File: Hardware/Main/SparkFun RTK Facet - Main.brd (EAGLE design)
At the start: 60 x 43 mm, 124 parts, among them J1 QWIIC_RIGHT_ANGLE, J2 U.FL, J9 CORTEX_JTAG_DEBUG_PTH, Q2 MBT3904DW1T1, Q3 SIL2308, U1 74HC4052D, U10 MCP73833, U12 AP2112K-3.3, U2 3.3V, U3 U-BLOX_ZED-F9P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

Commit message: Change to NO jumper for I2C pullups
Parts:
- added U$15, U$16: (no value), output:RTK5#SVG0
- C20: value 22uF -> 10uF
- JP7: value JUMPER-SMT_3_2-NC_TRACE_SILK -> JUMPER-SMT_3_NO_SILK; device SparkFun-Jumpers:SMT-JUMPER_3_2-NC_TRACE_SILK -> SparkFun-Jumpers:SMT-JUMPER_3_NO_SILK
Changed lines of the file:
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@@
 <layers>
 <layer number="1" name="Top/Horz" color="4" fill="1" visible="yes" active="yes"/>
-<layer number="2" name="GND/Horz" color="1" fill="3" visible="yes" active="yes"/>
-<layer number="15" name="3.3V/Vert" color="4" fill="6" visible="yes" active="yes"/>
+<layer number="2" name="GND/Horz" color="1" fill="3" visible="no" active="yes"/>
+<layer number="15" name="3.3V/Vert" color="4" fill="6" visible="no" active="yes"/>
 <layer number="16" name="Bottom/Vert" color="1" fill="1" visible="yes" active="yes"/>
 <layer number="17" name="Pads" color="2" fill="1" visible="yes" active="yes"/>
@@
 <layer number="23" name="tOrigins" color="15" fill="1" visible="yes" active="yes"/>
 <layer number="24" name="bOrigins" color="15" fill="1" visible="yes" active="yes"/>
-<layer number="25" name="tNames" color="7" fill="1" visible="yes" active="yes"/>
-<layer number="26" name="bNames" color="7" fill="1" visible="yes" active="yes"/>
-<layer number="27" name="tValues" color="7" fill="1" visible="yes" active="yes"/>
-<layer number="28" name="bValues" color="7" fill="1" visible="yes" active="yes"/>
-<layer number="29" name="tStop" color="7" fill="3" visible="yes" active="yes"/>
-<layer number="30" name="bStop" color="7" fill="6" visible="yes" active="yes"/>
-<layer number="31" name="tCream" color="7" fill="4" visible="yes" active="yes"/>
-<layer number="32" name="bCream" color="7" fill="5" visible="yes" active="yes"/>
-<layer number="33" name="tFinish" color="6" fill="3" visible="yes" active="yes"/>
-<layer number="34" name="bFinish" color="6" fill="6" visible="yes" active="yes"/>
-<layer number="35" name="tGlue" color="7" fill="4" visible="yes" active="yes"/>
-<layer number="36" name="bGlue" color="7" fill="5" visible="yes" active="yes"/>
-<layer number="37" name="tTest" color="7" fill="1" visible="yes" active="yes"/>
-<layer number="38" name="bTest" color="7" fill="1" visible="yes" active="yes"/>
-<layer number="39" name="tKeepout" color="4" fill="11" visible="yes" active="yes"/>
-<layer number="40" name="bKeepout" color="1" fill="11" visible="yes" active="yes"/>
-<layer number="41" name="tRestrict" color="4" fill="10" visible="yes" active="yes"/>
-<layer number="42" name="bRestrict" color="1" fill="10" visible="yes" active="yes"/>
-<layer number="43" name="vRestrict" color="2" fill="10" visible="yes" active="yes"/>
-<layer number="44" name="Drills" color="7" fill="1" visible="yes" active="yes"/>
+<layer number="25" name="tNames" color="7" fill="1" visible="no" active="yes"/>
+<layer number="26" name="bNames" color="7" fill="1" visible="no" active="yes"/>
+<layer number="27" name="tValues" color="7" fill="1" visible="no" active="yes"/>
+<layer number="28" name="bValues" color="7" fill="1" visible="no" active="yes"/>
+<layer number="29" name="tStop" color="7" fill="3" visible="no" active="yes"/>
+<layer number="30" name="bStop" color="7" fill="6" visible="no" active="yes"/>
+<layer number="31" name="tCream" color="7" fill="4" visible="no" active="yes"/>
+<layer number="32" name="bCream" color="7" fill="5" visible="no" active="yes"/>
+<layer number="33" name="tFinish" color="6" fill="3" visible="no" active="yes"/>
+<layer number="34" name="bFinish" color="6" fill="6" visible="no" active="yes"/>
+<layer number="35" name="tGlue" color="7" fill="4" visible="no" active="yes"/>
+<layer number="36" name="bGlue" color="7" fill="5" visible="no" active="yes"/>
+<layer number="37" name="tTest" color="7" fill="1" visible="no" active="yes"/>
+<layer number="38" name="bTest" color="7" fill="1" visible="no" active="yes"/>
+<layer number="39" name="tKeepout" color="4" fill="11" visible="no" active="yes"/>
+<layer number="40" name="bKeepout" color="1" fill="11" visible="no" active="yes"/>
+<layer number="41" name="tRestrict" color="4" fill="10" visible="no" active="yes"/>
+<layer number="42" name="bRestrict" color="1" fill="10" visible="no" active="yes"/>
+<layer number="43" name="vRestrict" color="2" fill="10" visible="no" active="yes"/>
+<layer number="44" name="Drills" color="7" fill="1" visible="no" active="yes"/>
 <layer number="45" name="Holes" color="7" fill="1" visible="yes" active="yes"/>
-<layer number="46" name="Milling" color="3" fill="1" visible="yes" active="yes"/>
-<layer number="47" name="Measures" color="7" fill="1" visible="yes" active="yes"/>
-<layer number="48" name="Document" color="7" fill="1" visible="yes" active="yes"/>
-<layer number="49" name="Reference" color="7" fill="1" visible="yes" active="yes"/>
-<layer number="50" name="dxf" color="7" fill="1" visible="yes" active="yes"/>
+<layer number="46" name="Milling" color="3" fill="1" visible="no" active="yes"/>
+<layer number="47" name="Measures" color="7" fill="1" visible="no" active="yes"/>
+<layer number="48" name="Document" color="7" fill="1" visible="no" active="yes"/>
+<layer number="49" name="Reference" color="7" fill="1" visible="no" active="yes"/>
+<layer number="50" name="dxf" color="7" fill="1" visible="no" active="yes"/>
 <layer number="51" name="tDocu" color="6" fill="1" visible="yes" active="yes"/>
-<layer number="52" name="bDocu" color="7" fill="1" visible="yes" active="yes"/>
+<layer number="52" name="bDocu" color="7" fill="1" visible="no" active="yes"/>
 <layer number="91" name="Nets" color="2" fill="1" visible="no" active="no"/>
 <layer number="92" name="Busses" color="1" fill="1" visible="no" active="no"/>
@@
 <attribute name="VALUE" x="19" y="11.762" size="0.6096" layer="28" font="vector" ratio="20" rot="MR180" align="top-center"/>
 </element>
-<element name="JP7" library="SparkFun-Jumpers" package="SMT-JUMPER_3_2-NC_TRACE_SILK" package3d_urn="urn:adsk.eagle:package:39289/1" value="JUMPER-SMT_3_2-NC_TRACE_SILK" x="22" y="10" smashed="yes" rot="MR270">
+<element name="JP7" library="SparkFun-Jumpers" package="SMT-JUMPER_3_NO_SILK" package3d_urn="urn:adsk.eagle:package:39285/1" value="JUMPER-SMT_3_NO_SILK" x="22" y="10" smashed="yes" rot="MR270">
 <attribute name="NAME" x="20.857" y="10" size="0.6096" layer="26" font="vector" ratio="20" rot="MR270" align="bottom-center"/>
 <attribute name="VALUE" x="23.143" y="10" size="0.6096" layer="28" font="vector" ratio="20" rot="MR270" align="top-center"/>
@@
 <attribute name="VALUE" x="6" y="30.778" size="0.6096" layer="28" font="vector" ratio="20" rot="MR180" align="top-center"/>
 </element>
-<element name="C20" library="SparkFun-Capacitors" package="0603" value="22uF" x="6" y="26" smashed="yes" rot="MR0">
+<element name="C20" library="SparkFun-Capacitors" package="0603" value="10uF" x="6" y="26" smashed="yes" rot="MR0">
 <attribute name="NAME" x="6" y="26.762" size="0.6096" layer="26" font="vector" ratio="20" rot="MR0" align="bottom-center"/>
-<attribute name="PROD_ID" value="CAP-14464" x="11" y="32" size="1.778" layer="28" font="vector" ratio="15" rot="MR0" display="off"/>
-<attribute name="VALUE" x="6" y="25.238" size="0.6096" layer="28" font="vector" ratio="20" rot="MR0" align="top-center"/>
+<attribute name="PROD_ID" value="CAP-11015" x="11" y="32" size="1.778" layer="28" font="vector" ratio="15" rot="MR0" display="off"/>
+<attribute name="VALUE" value="10uF" x="6" y="25.238" size="0.6096" layer="28" font="vector" ratio="20" rot="MR0" align="top-center"/>
 </element>
 <element name="R22" library="SparkFun-Resistors" package="0603" value="10k" x="6" y="24" smashed="yes" rot="MR180">
@@
 <element name="U$13" library="output" package="RTK_FACET0" value="" x="41.45" y="26.175" smashed="yes" rot="MR0"/>
 <element name="U$14" library="output" package="#GND#1" value="" x="52" y="11" smashed="yes" rot="MR270"/>
+<element name="U$15" library="output" package="RTK5#SVG0" value="" x="56.007" y="5.842" smashed="yes"/>
+<element name="U$16" library="output" package="RTK5#SVG0" value="" x="46.99" y="33.274" smashed="yes" rot="MR0"/>
 </elements>
 <signals>
@@
 <contactref element="R7" pad="2"/>
 <contactref element="JP7" pad="3"/>
-<wire x1="22" y1="8.9586" x2="19.8914" y2="8.9586" width="0.127" layer="16"/>
 <wire x1="19.8914" y1="8.9586" x2="19.85" y2="9" width="0.127" layer="16"/>
+<wire x1="22" y1="9.1872" x2="20.12" y2="9.1872" width="0.127" layer="16"/>
+<wire x1="20.12" y1="9.1872" x2="19.8914" y2="8.9586" width="0.127" layer="16"/>
 </signal>
 <signal name="N$4">
 <contactref element="R12" pad="2"/>
 <contactref element="JP7" pad="1"/>
-<wire x1="19.85" y1="11" x2="21.9586" y2="11" width="0.127" layer="16"/>
-<wire x1="21.9586" y1="11" x2="22" y2="11.0414" width="0.127" layer="16"/>
+<wire x1="22" y1="10.8128" x2="20.0372" y2="10.8128" width="0.127" layer="16"/>
+<wire x1="20.0372" y1="10.8128" x2="19.85" y2="11" width="0.127" layer="16"/>
 </signal>
 <signal name="N$5">

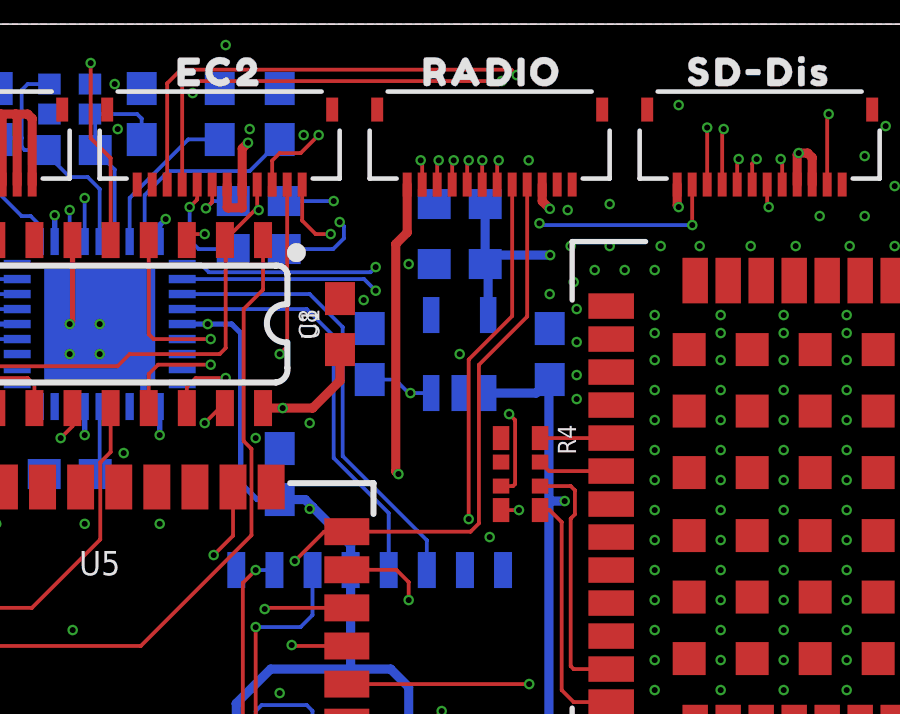
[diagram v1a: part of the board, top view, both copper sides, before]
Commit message: Double up 3.3V rail on Radio connector.
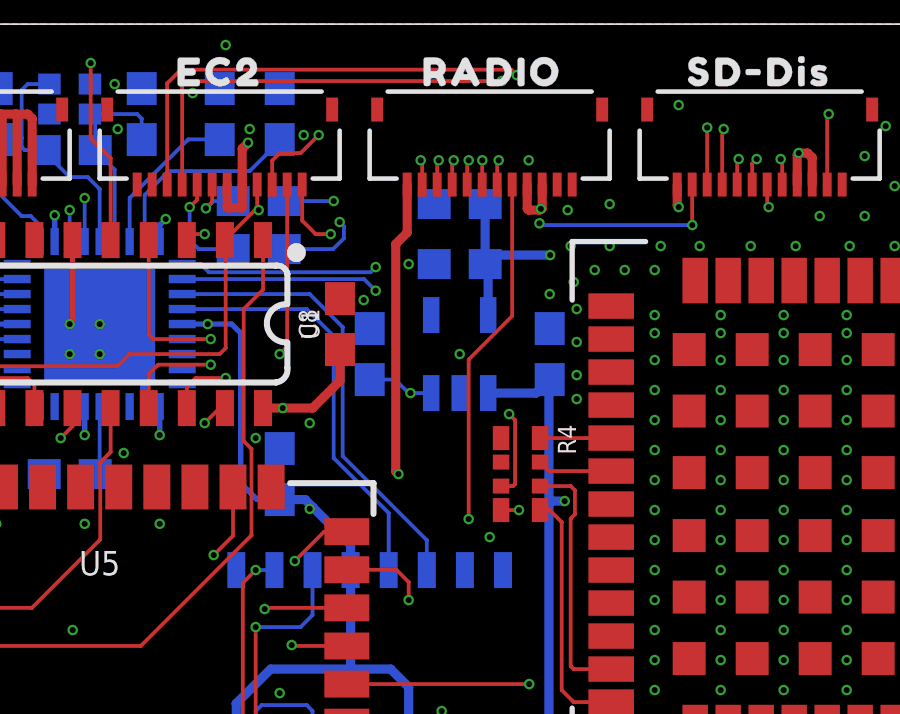
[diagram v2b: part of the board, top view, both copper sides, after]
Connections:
- removed net ESP_12/MTDI/RADIO_NI: J10.4, J9.8, U5.14
- new net ESP_12/MTDI: J9.8, U5.14
- net 3.3V: now also J10.4
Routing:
- net ESP_12/MTDI/RADIO_NI: track 43.0 -> 0.00 mm, vias 2 -> 0
- net ESP_12/MTDI: track 0.00 -> 26.5 mm, vias 0 -> 2
- net 3.3V: track 29.8 -> 31.0 mm
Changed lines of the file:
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@@
 <layers>
 <layer number="1" name="Top/Horz" color="4" fill="1" visible="yes" active="yes"/>
-<layer number="2" name="GND/Horz" color="1" fill="3" visible="no" active="yes"/>
-<layer number="15" name="3.3V/Vert" color="4" fill="6" visible="no" active="yes"/>
+<layer number="2" name="GND/Horz" color="1" fill="3" visible="yes" active="yes"/>
+<layer number="15" name="3.3V/Vert" color="4" fill="6" visible="yes" active="yes"/>
 <layer number="16" name="Bottom/Vert" color="1" fill="1" visible="yes" active="yes"/>
 <layer number="17" name="Pads" color="2" fill="1" visible="yes" active="yes"/>
@@
 <layer number="39" name="tKeepout" color="4" fill="11" visible="no" active="yes"/>
 <layer number="40" name="bKeepout" color="1" fill="11" visible="no" active="yes"/>
-<layer number="41" name="tRestrict" color="4" fill="10" visible="no" active="yes"/>
+<layer number="41" name="tRestrict" color="4" fill="10" visible="yes" active="yes"/>
 <layer number="42" name="bRestrict" color="1" fill="10" visible="no" active="yes"/>
 <layer number="43" name="vRestrict" color="2" fill="10" visible="no" active="yes"/>
@@
 <dimension x1="0" y1="0" x2="0" y2="43" x3="-2" y3="21.5" textsize="1" textratio="15" layer="47" width="0.08"/>
 <dimension x1="0" y1="43" x2="60" y2="43" x3="30" y3="47" textsize="1" textratio="15" layer="47" width="0.08"/>
+<rectangle x1="9.4" y1="35.5" x2="9.6" y2="35.8" layer="41"/>
+<rectangle x1="9.9" y1="35.5" x2="10.1" y2="35.8" layer="41"/>
+<rectangle x1="18.4" y1="35.5" x2="18.6" y2="35.8" layer="41"/>
+<rectangle x1="32.4" y1="35.5" x2="32.6" y2="35.8" layer="41"/>
+<rectangle x1="10.4" y1="35.5" x2="10.5" y2="35.8" layer="41"/>
+<rectangle x1="18.9" y1="35.5" x2="19.1" y2="35.8" layer="41"/>
+<rectangle x1="32" y1="35.5" x2="32.1" y2="35.8" layer="41"/>
 </plain>
 <attributes>
@@
 <wire x1="40.3" y1="36.7" x2="40.6" y2="36.7" width="0.3048" layer="1"/>
 <contactref element="J10" pad="3"/>
-<wire x1="31.75" y1="35.65" x2="31.75" y2="35.0953" width="0.3048" layer="1"/>
-<wire x1="31.75" y1="35.0953" x2="32.004" y2="34.8413" width="0.3048" layer="1"/>
-<via x="32.004" y="34.8413" extent="1-16" drill="0.2"/>
+<via x="31.704" y="34.8413" extent="1-16" drill="0.2"/>
+<contactref element="J10" pad="4"/>
+<wire x1="31.25" y1="35.65" x2="31.25" y2="34.85" width="0.3048" layer="1"/>
+<wire x1="31.25" y1="34.85" x2="31.3" y2="34.8" width="0.3048" layer="1"/>
+<wire x1="31.6627" y1="34.8" x2="31.3" y2="34.8" width="0.3048" layer="1"/>
+<wire x1="31.75" y1="34.85" x2="31.75" y2="35.65" width="0.3048" layer="1"/>
+<wire x1="31.704" y1="34.8413" x2="31.6627" y2="34.8" width="0.3048" layer="1"/>
+<wire x1="31.704" y1="34.8413" x2="31.7127" y2="34.85" width="0.3048" layer="1"/>
+<wire x1="31.7127" y1="34.85" x2="31.75" y2="34.85" width="0.3048" layer="1"/>
 </signal>
 <signal name="GND">
@@
 <wire x1="27.3" y1="22.4" x2="27.3" y2="21.8" width="0.127" layer="1"/>
 </signal>
-<signal name="ESP_12/MTDI/RADIO_NI">
+<signal name="ESP_12/MTDI">
 <contactref element="U5" pad="14"/>
 <contactref element="J9" pad="8"/>
-<contactref element="J10" pad="4"/>
 <via x="23" y="18.7" extent="1-16" drill="0.2"/>
 <wire x1="3.635" y1="17.73" x2="9.406025" y2="17.73" width="0.127" layer="2"/>
@@
 <wire x1="23.5028" y1="23.1" x2="24.4828" y2="24.08" width="0.127" layer="1"/>
 <wire x1="24.4828" y1="24.08" x2="25.238" y2="24.08" width="0.127" layer="1"/>
-<wire x1="31.25" y1="35.65" x2="31.25" y2="31.25" width="0.127" layer="1"/>
-<wire x1="31.25" y1="31.25" x2="29.6413" y2="29.6413" width="0.127" layer="1"/>
-<wire x1="29.6413" y1="29.6413" x2="29.6413" y2="24.358625" width="0.127" layer="1"/>
-<wire x1="25.238" y1="24.08" x2="29.362675" y2="24.08" width="0.127" layer="1"/>
-<wire x1="29.362675" y1="24.08" x2="29.6413" y2="24.358625" width="0.127" layer="1"/>
 </signal>
 <signal name="ESP_3V3" class="1">
